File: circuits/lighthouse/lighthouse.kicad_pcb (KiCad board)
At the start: 2 copper layers, 83 x 80 mm, 81 parts, among them IC1 SX1308, J1 USB_C_Receptacle_USB2.0_14P, Q1 S9013, Q2 FS8205A, Q3 2N7002K, Q4 SS8050, Q5 SS8050, U1 R300, U10 CP2102-GMR, U2 AMS1117-3.3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

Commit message: Sorted out pcb layers
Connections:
- Q2 pad 5: GND -> Net-(Q2-G2)
- R5 pad 1: Net-(U5-VCC) -> /Charger/+BAT
- R5 pad 2: /Charger/+BAT -> Net-(U5-VCC)
- R6 pad 1: Net-(U5-CS) -> GND
- R6 pad 2: GND -> Net-(U5-CS)
- U5 pad 3: GND -> Net-(Q2-G2)
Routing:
- net GND: track 127.6 -> 114.9 mm, vias 16 -> 14
- net Net-(Q2-G2): track 0.00 -> 12.8 mm, vias 0 -> 2

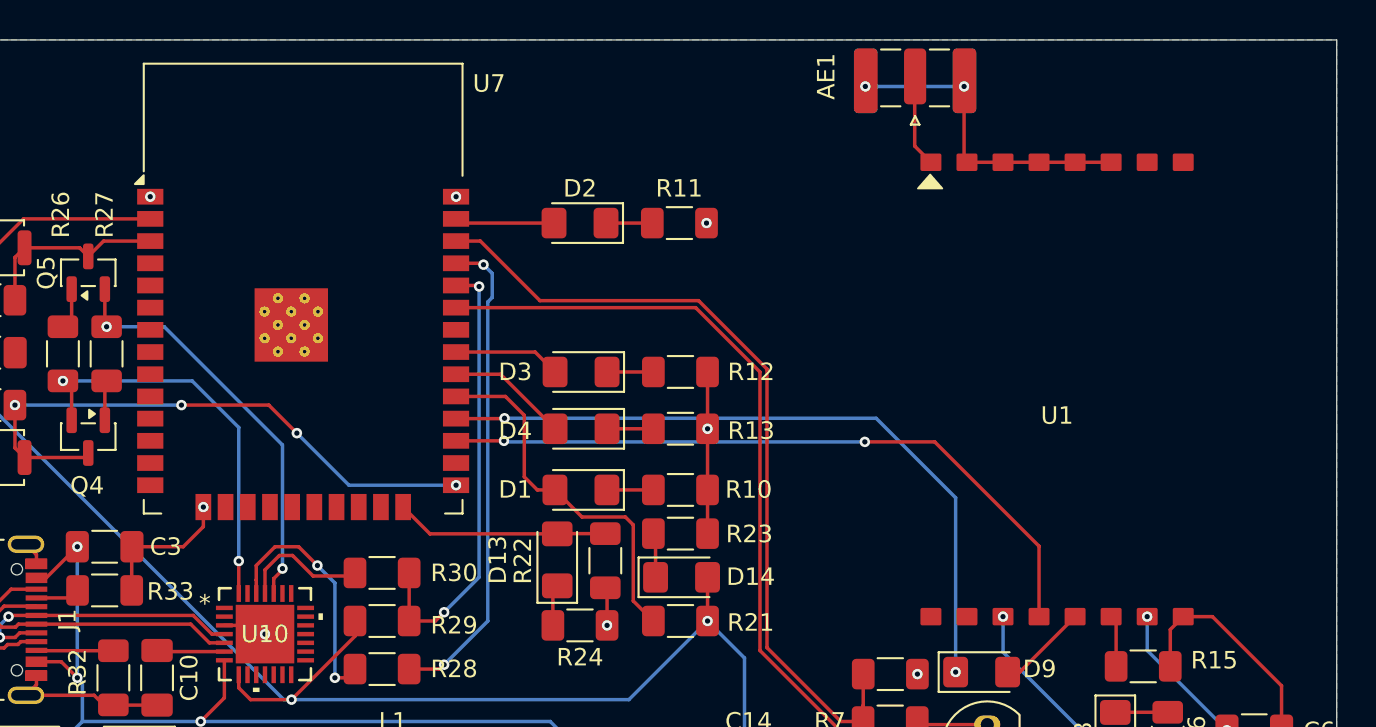
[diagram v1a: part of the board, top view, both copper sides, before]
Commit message: Added the buttons some dingus forgot
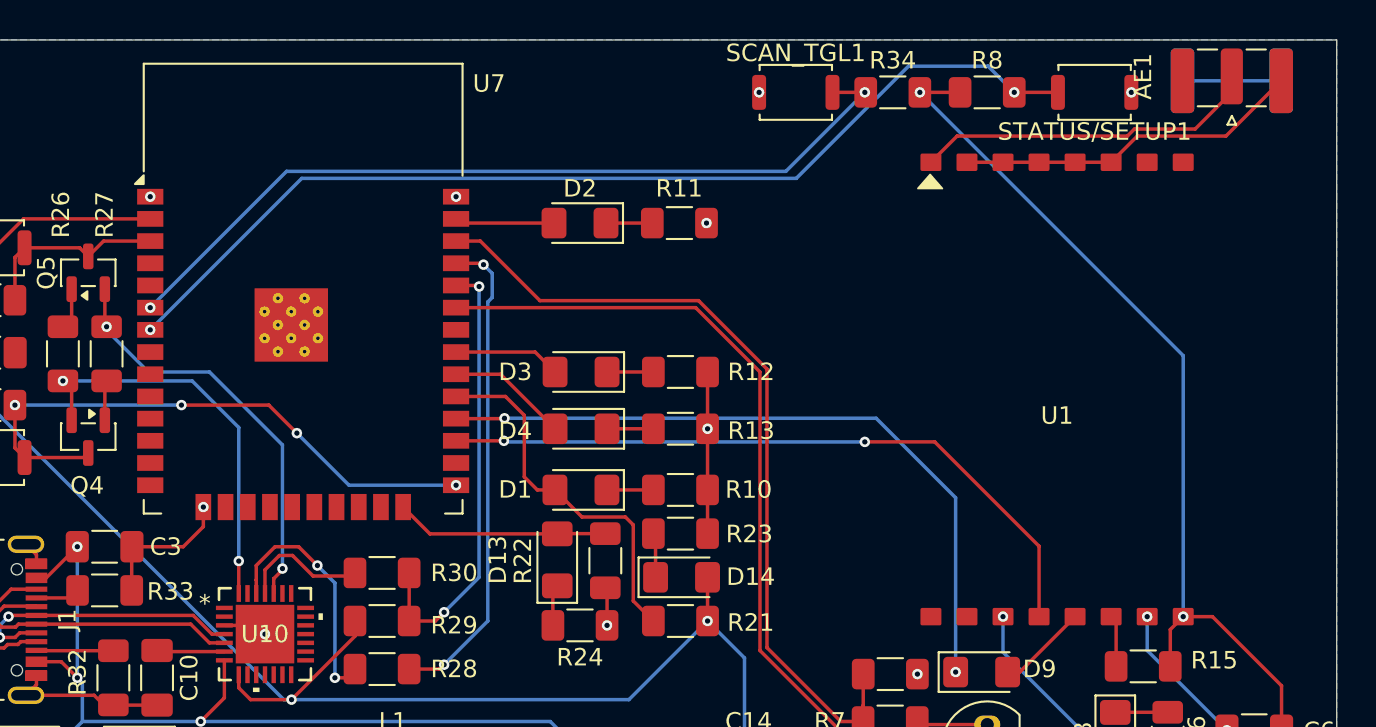
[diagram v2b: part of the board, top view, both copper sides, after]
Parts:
- added R34: 10k, Resistor_SMD:R_1206_3216Metric_Pad1.30x1.75mm_HandSolder, F.Cu at (91.6, 67.0)
- added R8: 10k, Resistor_SMD:R_1206_3216Metric_Pad1.30x1.75mm_HandSolder, F.Cu at (97.0, 67.0)
- added SCAN_TGL1: SW_Push, Button_Switch_SMD:SW_Push_SPST_NO_Alps_SKRK, F.Cu at (86.0, 67.0)
- added STATUS/SETUP1: SW_Push, Button_Switch_SMD:SW_Push_SPST_NO_Alps_SKRK, F.Cu at (103.2, 67.0)
- moved AE1 18.1 mm to (111.0, 66.1)
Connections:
- U7 pad 6: unconnected-(U7-IO34-Pad6) -> Net-(U7-IO34)
- U7 pad 7: unconnected-(U7-IO35-Pad7) -> Net-(U7-IO35)
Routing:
- net Net-(U7-IO35): track 0.00 -> 58.8 mm, vias 0 -> 2
- net Net-(U7-IO34): track 0.00 -> 47.9 mm, vias 0 -> 2
- net +5V: track 166.1 -> 204.6 mm, vias 7 -> 9
- net Net-(AE1-A): track 4.97 -> 19.8 mm
- net Net-(AE1-Shield): track 18.3 -> 25.8 mm, vias 2 -> 0
- net GND: vias 14 -> 16

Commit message: Pre-pin reassignment commit
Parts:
- added J2: Conn_01x03_Socket, Connector_JST:JST_XH_B3B-XH-A_1x03_P2.50mm_Vertical, F.Cu at (74.0, 80.0)
- moved D1 3.75 mm to (73.8, 93.5)
- moved D13 3.75 mm to (72.4, 97.5)
- moved D14 3.75 mm to (79.5, 98.5)
- moved D3 3.75 mm to (73.8, 86.8)
- moved D4 3.75 mm to (73.8, 90.0)
- moved R10 3.75 mm to (79.5, 93.5)
- moved R12 3.75 mm to (79.5, 86.8)
- moved R13 3.75 mm to (79.5, 90.0)
- moved R21 3.75 mm to (79.5, 101.0)
- moved R22 3.75 mm to (75.2, 97.5)
- moved R23 3.75 mm to (79.5, 96.0)
- moved R24 3.75 mm to (73.7, 101.2)
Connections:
- U7 pad 8: unconnected-(U7-IO32-Pad8) -> PIR
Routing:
- net ACTIVE_SCAN: track 6.96 -> 10.7 mm
- net MQTT_STS: track 21.2 -> 24.4 mm
- net SCAN_DETECTED: track 6.37 -> 8.79 mm
- net RFID_PW: track 44.1 -> 46.1 mm
- net ESP24: track 12.7 -> 14.3 mm

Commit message: Ready to go circuit (what a naive thing to say)
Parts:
- moved D4 14.3 mm to (73.4, 75.7)
- moved R13 14.3 mm to (79.0, 75.7)
- moved D3 13.6 mm to (73.4, 73.2)
- moved R12 13.6 mm to (79.0, 73.2)
- moved R21 7.28 mm to (73.1, 97.4), turned to 90 degrees
- moved D14 5.76 mm to (74.4, 101.2), turned to 180 degrees
- moved D13 5.03 mm to (67.4, 97.4)
- moved R10 5.03 mm to (74.4, 93.4)
- moved R22 5.03 mm to (70.1, 97.4)
- moved R24 5.03 mm to (68.7, 101.1)
- moved D1 5.03 mm to (68.7, 93.4)
- moved J2 4.65 mm to (76.8, 83.8)
- moved R23 4.01 mm to (75.7, 97.4), turned to -90 degrees
- moved D2 3.73 mm to (73.3, 78.2)
- moved R11 3.73 mm to (79.0, 78.2)
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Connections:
- R34 pad 1: Net-(U7-IO34) -> Net-(U7-IO23)
- R34 pad 2: +5V -> +3.3V
- R8 pad 1: +5V -> +3.3V
- R8 pad 2: Net-(U7-IO35) -> Net-(U7-IO22)
- SCAN_TGL1 pad 2: Net-(U7-IO34) -> Net-(U7-IO23)
- STATUS/SETUP1 pad 2: Net-(U7-IO35) -> Net-(U7-IO22)
- U7 pad 10: unconnected-(U7-IO25-Pad10) -> ESP25
- U7 pad 23: unconnected-(U7-IO15-Pad23) -> ESP34
- U7 pad 24: ESP24 -> ESP35
- U7 pad 25: ESP25 -> ESP24
- U7 pad 26: unconnected-(U7-IO4-Pad26) -> MQTT_STS
- U7 pad 29: MQTT_STS -> RFID_PW
- U7 pad 30: ACTIVE_SCAN -> RFID_PW_SENSE
- U7 pad 31: SCAN_DETECTED -> PIR
- U7 pad 33: RFID_PW -> WIFI_STS
- U7 pad 34: ESP34 -> ACTIVE_SCAN
- U7 pad 35: ESP35 -> SCAN_DETECTED
- U7 pad 36: RFID_PW_SENSE -> Net-(U7-IO22)
- U7 pad 37: WIFI_STS -> Net-(U7-IO23)
- U7 pad 6: Net-(U7-IO34) -> unconnected-(U7-IO34-Pad6)
- U7 pad 7: Net-(U7-IO35) -> unconnected-(U7-IO35-Pad7)
- U7 pad 8: PIR -> unconnected-(U7-IO32-Pad8)
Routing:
- net Net-(U7-IO35): track 58.8 -> 0.00 mm, vias 2 -> 0
- net +5V: track 204.6 -> 263.3 mm, vias 9 -> 13
- net Net-(U7-IO34): track 47.9 -> 0.00 mm, vias 2 -> 0
- net +3.3V: track 109.9 -> 150.2 mm, vias 4 -> 6
- net GND: track 114.9 -> 75.4 mm, vias 16 -> 18
- net Net-(U7-IO22): track 0.00 -> 37.4 mm
- net Net-(U7-IO23): track 0.00 -> 28.1 mm
- net ESP25: track 34.6 -> 12.7 mm, vias 4 -> 0
- net ESP34: track 26.3 -> 9.00 mm, vias 2 -> 0
- net ESP35: track 27.9 -> 11.5 mm, vias 2 -> 0
- net PIR: track 0.00 -> 14.2 mm
- net RFID_PW_SENSE: track 46.7 -> 33.7 mm
- net RFID_PW: track 46.1 -> 33.5 mm
- net MQTT_STS: track 24.4 -> 15.5 mm
- net (no net): track 7.98 -> 0.00 mm
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
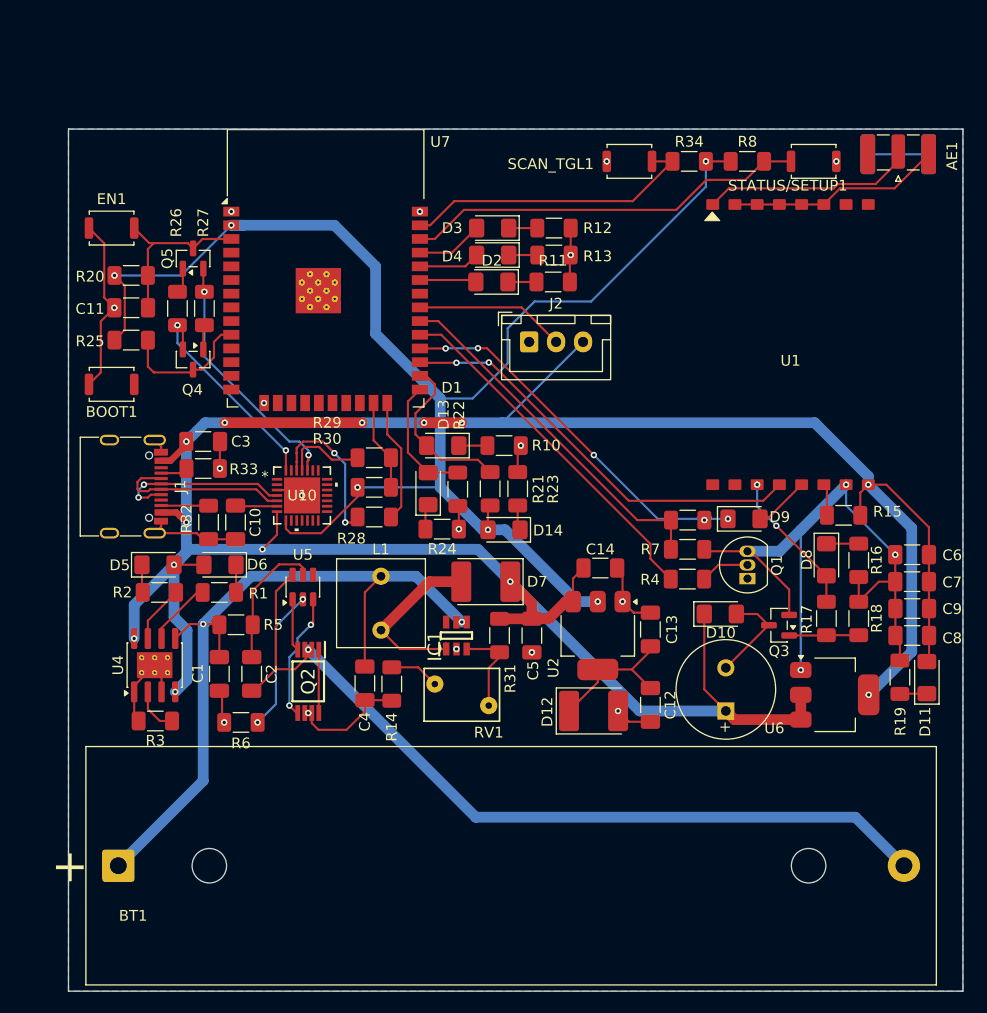
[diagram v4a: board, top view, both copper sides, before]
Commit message: Adjusted visa sizes
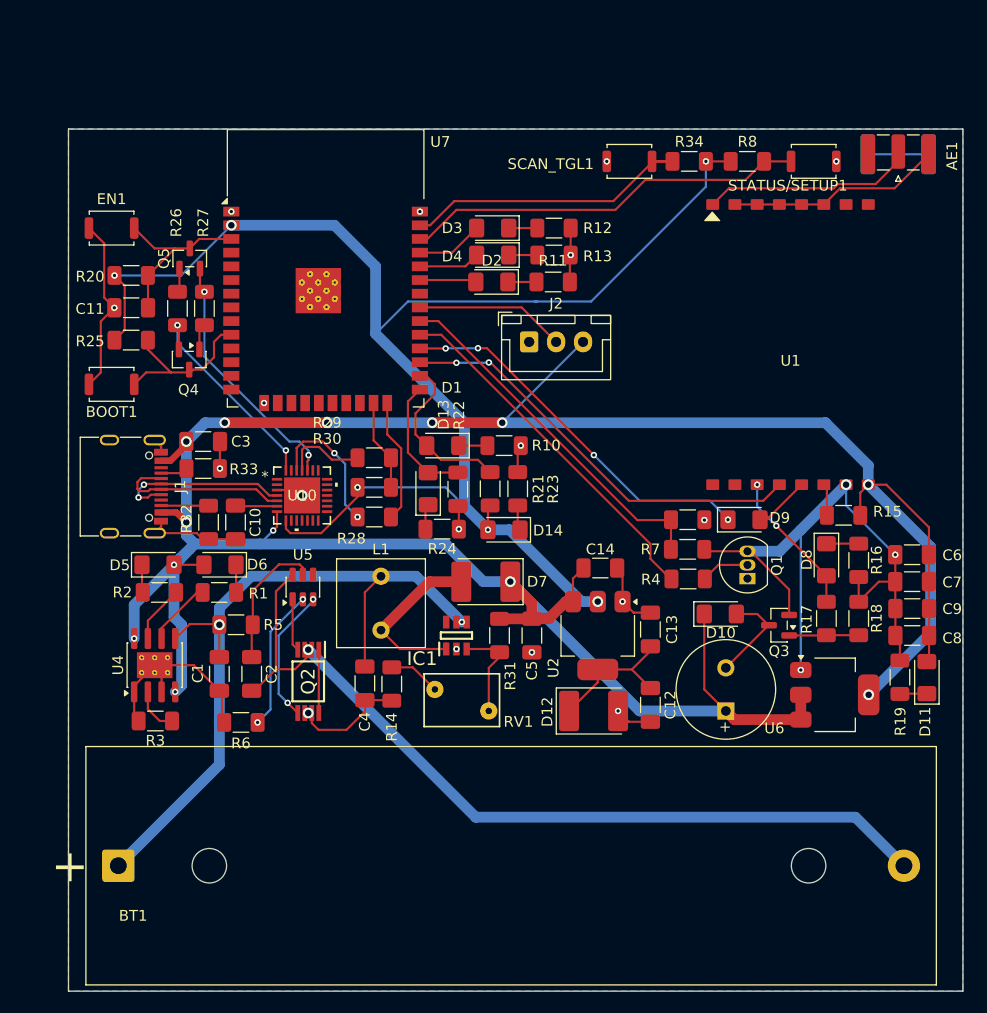
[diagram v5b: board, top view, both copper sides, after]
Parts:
- moved RV1 0.50 mm to (73.0, 118.0)
- moved Q4 0.36 mm to (45.2, 85.4)
- moved Q5 0.31 mm to (45.2, 76.0)
- moved D9 0.08 mm to (96.7, 100.2)
- moved R4 0.07 mm to (91.5, 105.8)
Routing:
- net GND: track 75.4 -> 81.5 mm, vias 18 -> 17
- net +3.3V: track 150.2 -> 153.7 mm
- net ESP25: track 12.7 -> 15.6 mm
- net Net-(U10-TXD): track 14.9 -> 13.5 mm
- net /Charger/+BAT: track 72.2 -> 70.9 mm
- net Net-(Q2-G2): track 11.8 -> 12.7 mm
- net +5V: track 263.3 -> 264.0 mm
- net Net-(Q5-B): track 2.36 -> 2.93 mm
- net MP28: track 20.2 -> 20.7 mm
- net Net-(IC1-FB): track 9.25 -> 9.75 mm

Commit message: Added YR300 model
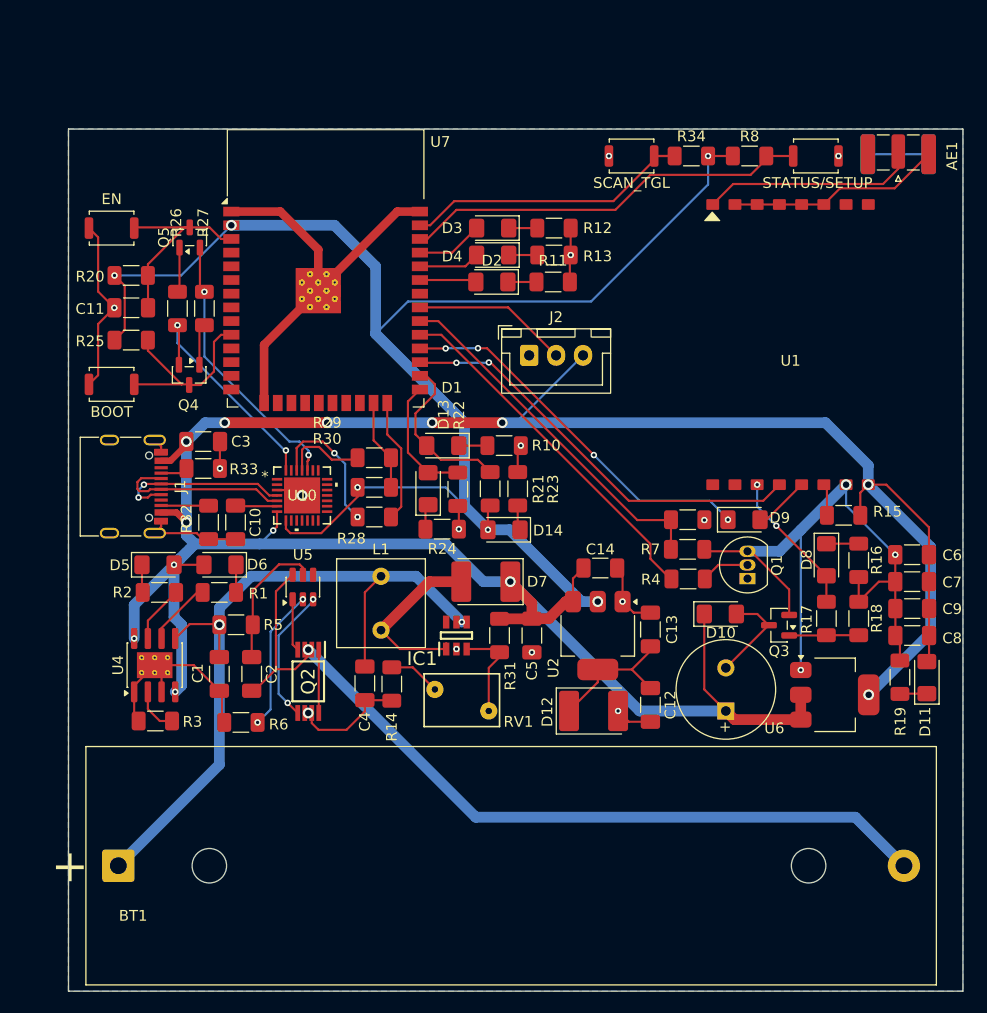
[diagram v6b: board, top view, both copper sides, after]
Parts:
- moved Q5 1.95 mm to (45.2, 74.1)
- moved Q4 1.42 mm to (45.2, 86.8)
- moved J2 1.25 mm to (76.8, 85.0)
- moved R34 0.54 mm to (91.8, 66.5)
- moved R8 0.54 mm to (97.2, 66.5)
- moved SCAN_TGL 0.54 mm to (86.2, 66.5)
- moved STATUS/SETUP 0.54 mm to (103.3, 66.5)
- renumbered BOOT1 to BOOT, EN1 to EN, SCAN_TGL1 to SCAN_TGL, STATUS/SETUP1 to STATUS/SETUP
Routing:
- net GND: track 81.5 -> 119.8 mm, vias 17 -> 14
- net ESP25: track 15.6 -> 18.0 mm
- net EN: track 16.7 -> 18.8 mm
- net Net-(Q5-B): track 2.93 -> 4.89 mm
- net MP24: track 23.5 -> 25.4 mm
- net Net-(Q4-B): track 2.44 -> 3.87 mm
- net MP28: track 20.7 -> 22.1 mm
- net +5V: track 264.0 -> 263.5 mm
- net PIR: track 14.2 -> 14.7 mm

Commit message: Moved dimension to the correct layer
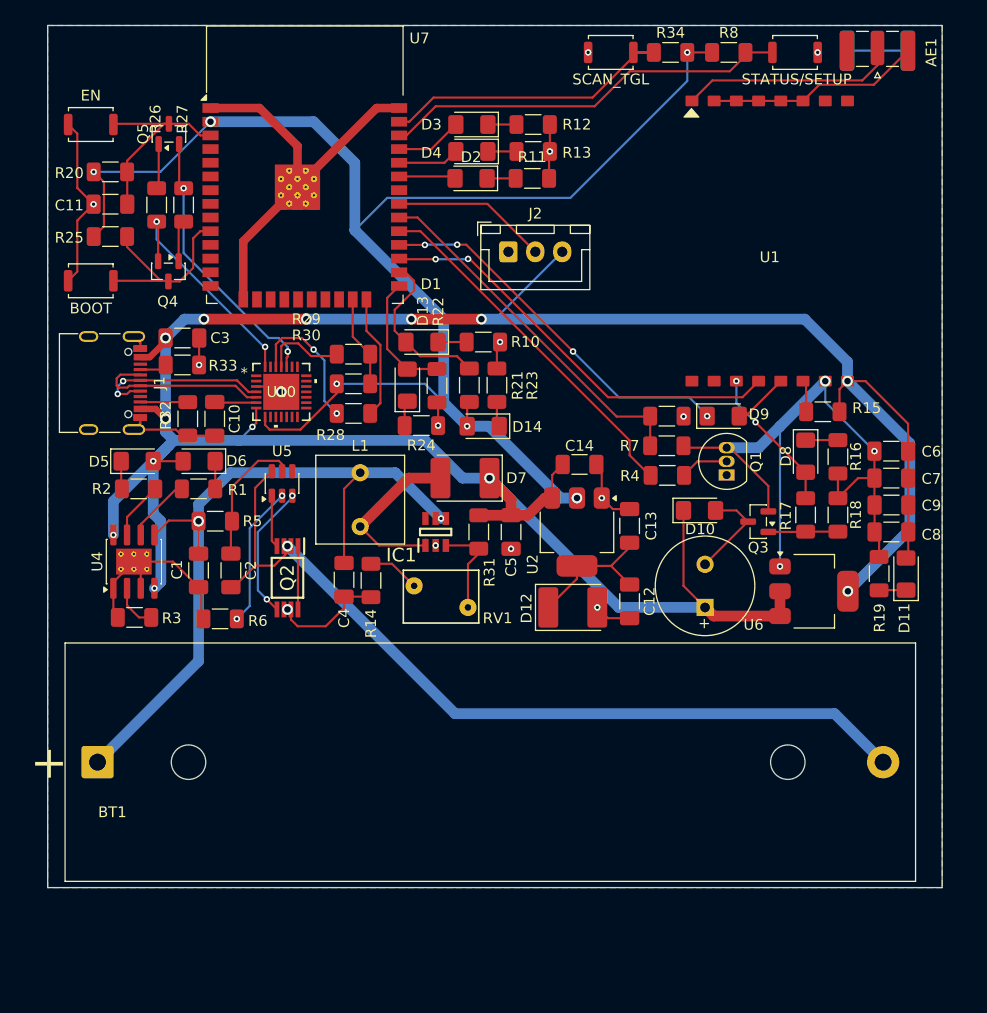
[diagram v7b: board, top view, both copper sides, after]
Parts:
- moved R17 9.80 mm to (102.4, 99.8)
- moved R18 9.80 mm to (105.4, 99.8)
- moved BT1 9.80 mm to (36.7, 122.8)
- moved J1 9.80 mm to (36.9, 87.6)
- moved Q1 9.80 mm to (95.1, 96.1)
- moved BZ1 9.80 mm to (93.1, 108.4)
- moved C12 9.80 mm to (86.1, 107.8)
- moved C13 9.80 mm to (86.1, 100.8)
- moved C5 9.80 mm to (75.1, 101.4)
- moved C6 9.80 mm to (110.4, 93.9)
- moved C7 9.80 mm to (110.4, 96.4)
- moved D1 9.80 mm to (66.8, 83.8)
- moved D13 9.80 mm to (65.4, 87.8)
- moved D8 9.80 mm to (102.4, 94.4)
- moved D9 9.80 mm to (94.8, 90.6)
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
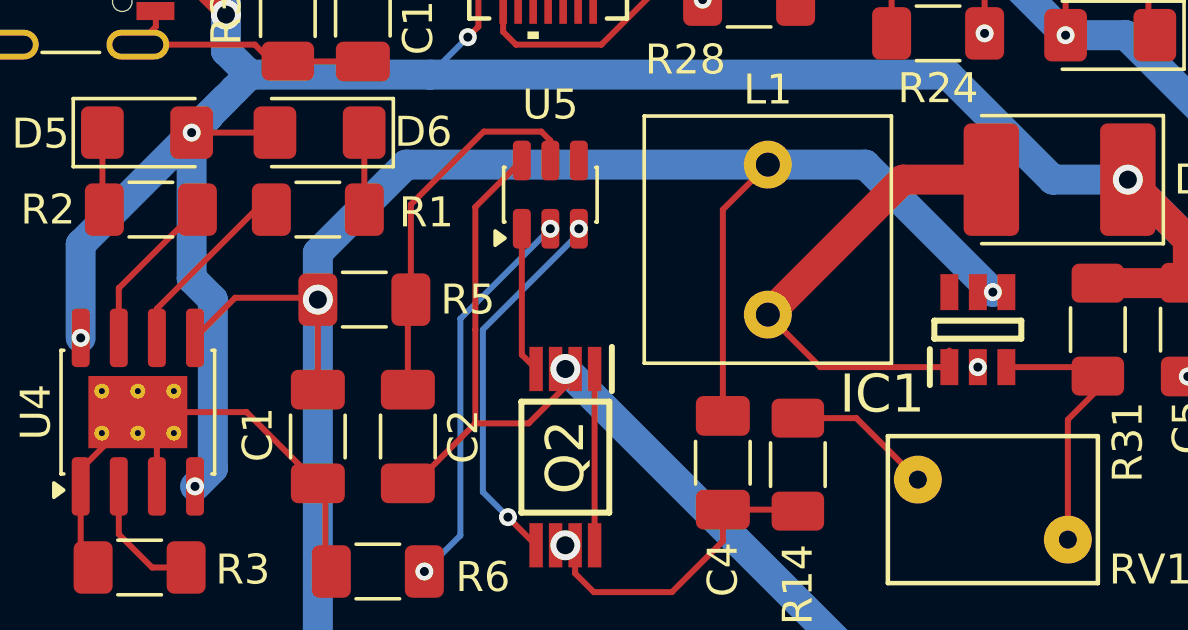
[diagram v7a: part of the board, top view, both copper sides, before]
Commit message: Added bulk capacitors, fuses and battery power sense
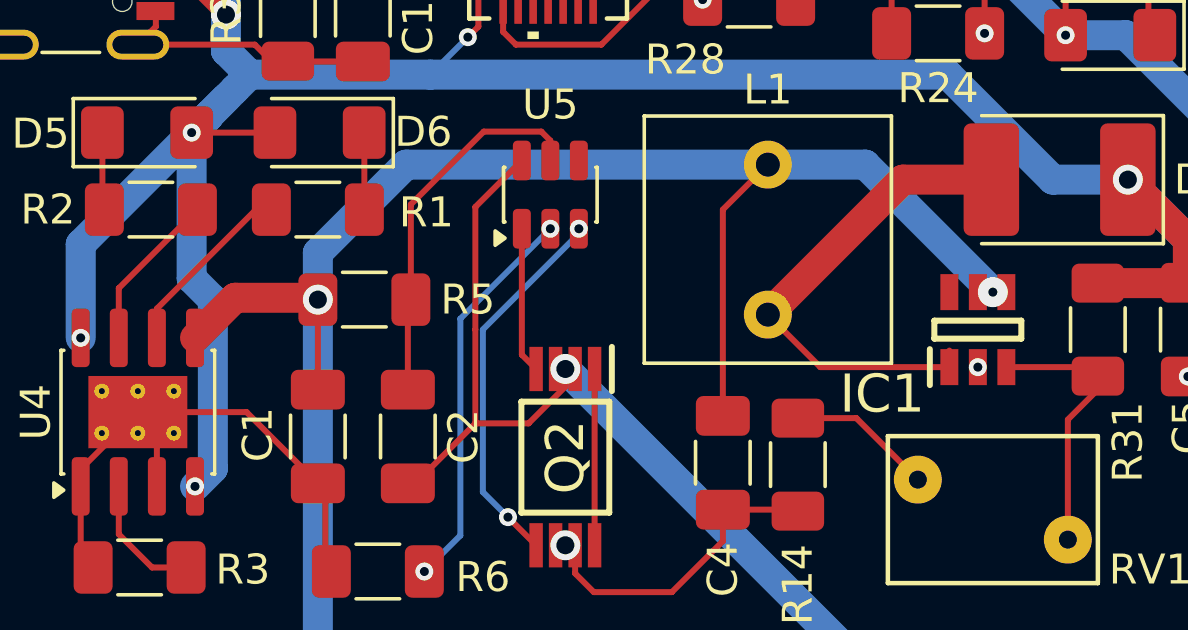
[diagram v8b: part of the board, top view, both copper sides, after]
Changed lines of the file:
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@@
 		(start 46.0075 100.3275)
 		(end 43.3125 100.3275)
-		(width 0.2)
+		(width 1)
 		(layer "F.Cu")
 		(net 1)
@@
 		(start 43.3125 100.3275)
 		(end 41.975 101.665)
-		(width 0.2)
+		(width 1)
 		(layer "F.Cu")
 		(net 1)
@@
 	(via
 		(at 68.57 100.14)
-		(size 0.6)
+		(size 1)
 		(drill 0.3)
 		(layers "F.Cu" "B.Cu")
